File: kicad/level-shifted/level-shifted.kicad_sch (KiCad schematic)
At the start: 7 parts, among them J104 PAL-1 Expansion Connector, SW101 PICO RESET, SW102 SW_DIP_x01, U104 Pico

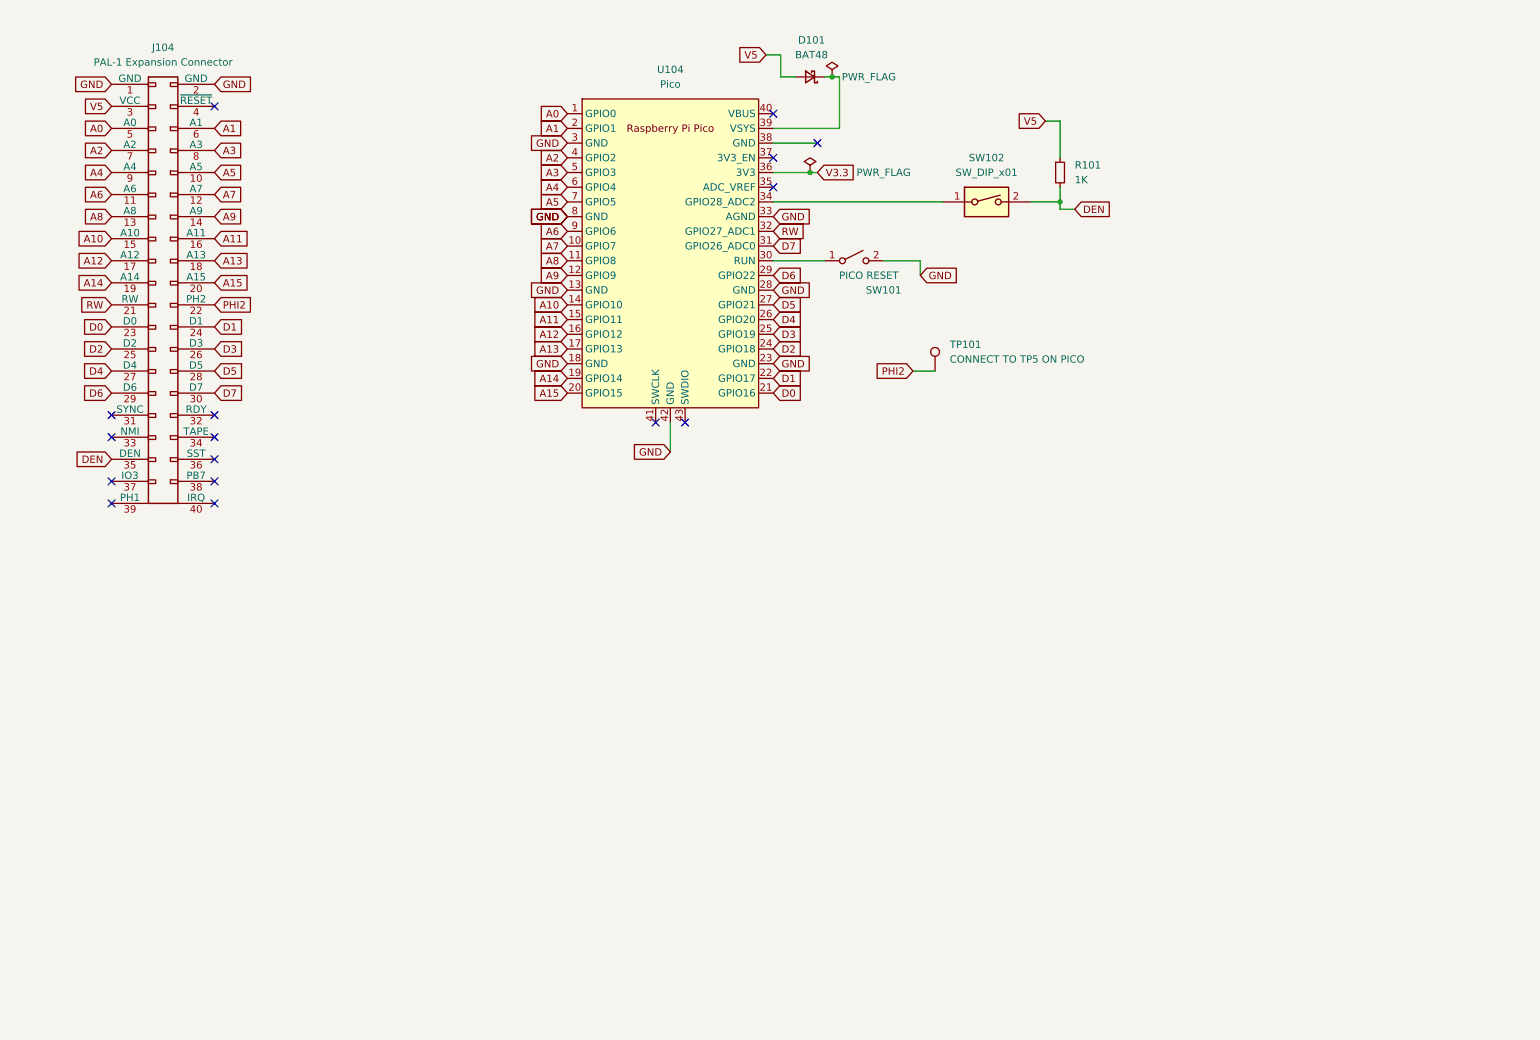
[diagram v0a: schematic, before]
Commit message: New board prepared with the level shifters in place
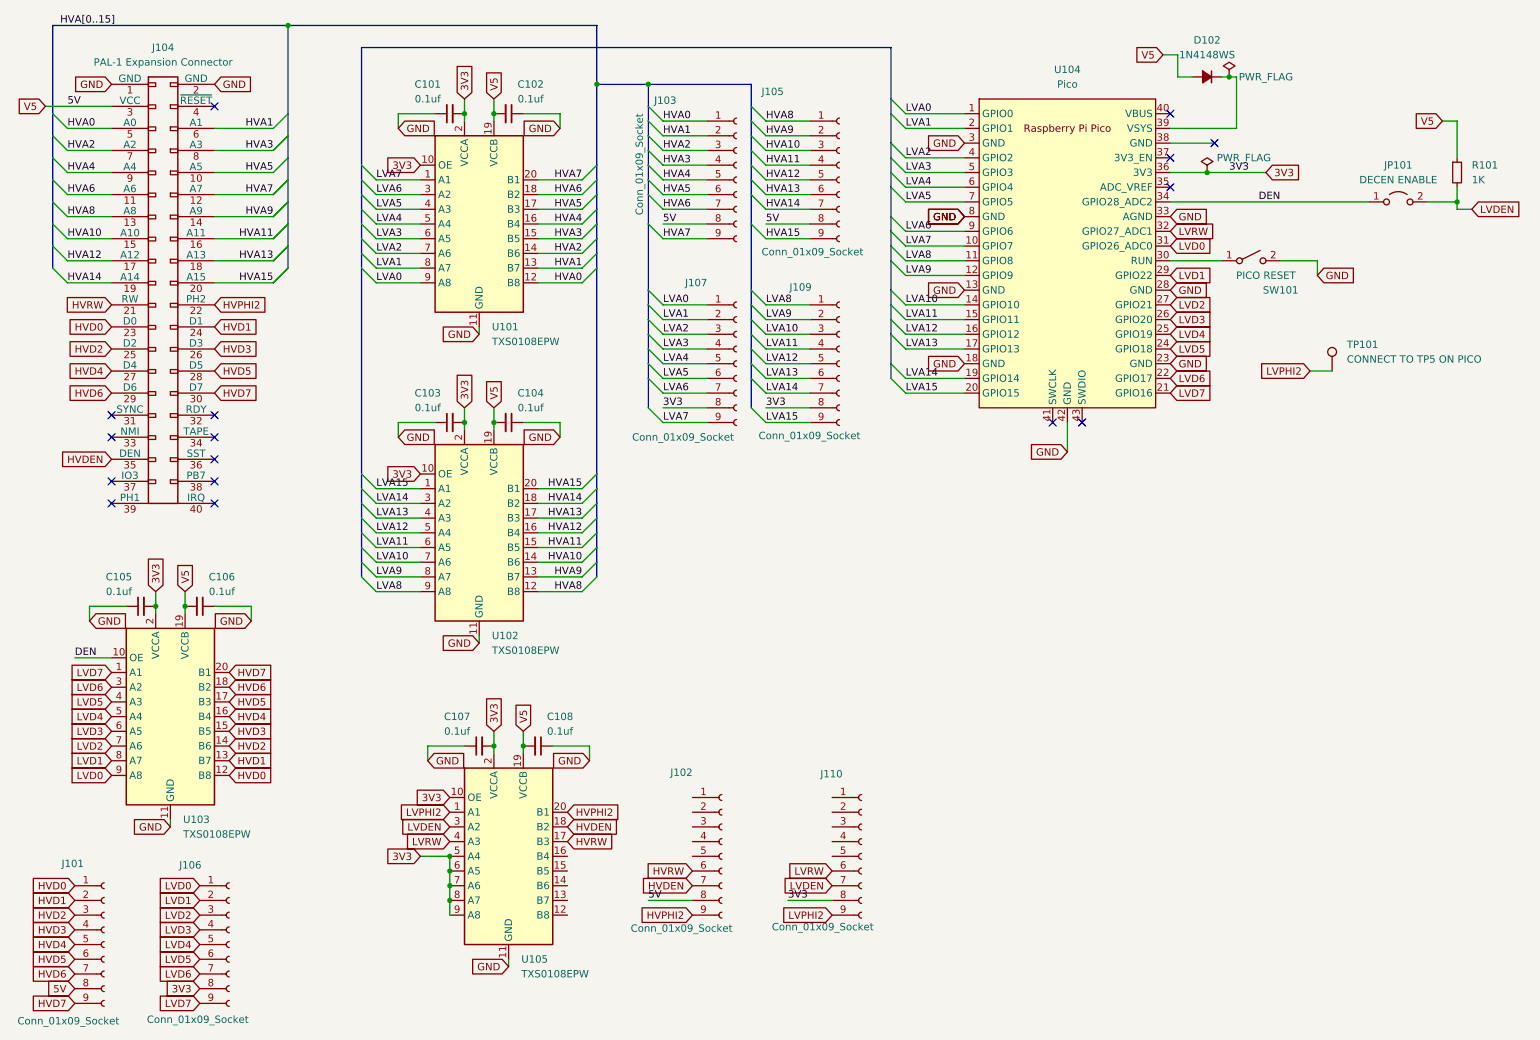
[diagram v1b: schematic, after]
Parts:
- removed D101: BAT48, Diode_THT:D_5W_P10.16mm_Horizontal, symbol Device:D_Schottky_Small
- removed SW102: SW_DIP_x01, Button_Switch_THT:SW_DIP_SPSTx01_Slide_9.78x4.72mm_W7.62mm_P2.54mm, symbol Switch:SW_DIP_x01
- added C101, C102, C103, C104, C105, C106, C107, C108: 0.1uf, Capacitor_SMD:C_0603_1608Metric_Pad1.08x0.95mm_HandSolder, symbol Device:C_Small
- added D102: 1N4148WS, Diode_SMD:D_SOD-323F, symbol Device:D_Small_Filled
- added J101, J102, J103, J105, J106, J107, J109, J110: Conn_01x09_Socket, Connector_PinHeader_1.27mm:PinHeader_1x09_P1.27mm_Vertical, symbol Connector:Conn_01x09_Socket
- added JP101: DECEN ENABLE, Jumper:SolderJumper-2_P1.3mm_Open_RoundedPad1.0x1.5mm, symbol Jumper:Jumper_2_Open
- added U101, U102, U103, U105: TXS0108EPW, Package_SO:TSSOP-20_4.4x6.5mm_P0.65mm, symbol Logic_LevelTranslator:TXS0108EPW
- R101: footprint Resistor_THT:R_Axial_DIN0207_L6.3mm_D2.5mm_P10.16mm_Horizontal -> Resistor_SMD:R_0603_1608Metric_Pad0.98x0.95mm_HandSolder
- SW101: footprint Button_Switch_THT:SW_PUSH_6mm -> Button_Switch_SMD:SW_Push_1P1T_XKB_TS-1187A; JLCPCB (none) -> C2845316; MFG (none) -> HCTL; MFG# (none) -> TC-6601-6-260G
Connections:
- net DEN: now also U104.34 (GPIO28_ADC2), JP101.1 (A), U103.10 (OE); no longer J104.35 (DEN), R101.2
- net GND: now also C101.1, C102.1, C103.1, C104.1, C105.1, C106.1, C107.1, C108.1, U101.11 (GND), U102.11 (GND), U103.11 (GND), U105.11 (GND)
- net at U104.39 (VSYS): now also D102.1 (K)
- net A0 renamed HVA0
- net HVA0: now also J103.1 (Pin_1), U101.12 (B8); no longer U104.1 (GPIO0)
- net A1 renamed HVA1
- net HVA1: now also J103.2 (Pin_2), U101.13 (B7); no longer U104.2 (GPIO1)
- net A10 renamed HVA10
- net HVA10: now also J105.3 (Pin_3), U102.14 (B6); no longer U104.14 (GPIO10)
- net A11 renamed HVA11
- net HVA11: now also J105.4 (Pin_4), U102.15 (B5); no longer U104.15 (GPIO11)
- net A12 renamed HVA12
- net HVA12: now also J105.5 (Pin_5), U102.16 (B4); no longer U104.16 (GPIO12)
- net A13 renamed HVA13
- net HVA13: now also J105.6 (Pin_6), U102.17 (B3); no longer U104.17 (GPIO13)
- net A14 renamed HVA14
- net HVA14: now also J105.7 (Pin_7), U102.18 (B2); no longer U104.19 (GPIO14)
- net A15 renamed HVA15
- net HVA15: now also J105.9 (Pin_9), U102.20 (B1); no longer U104.20 (GPIO15)
- net A2 renamed HVA2
- net HVA2: now also J103.3 (Pin_3), U101.14 (B6); no longer U104.4 (GPIO2)
- net A3 renamed HVA3
- net HVA3: now also J103.4 (Pin_4), U101.15 (B5); no longer U104.5 (GPIO3)
- net A4 renamed HVA4
- net HVA4: now also J103.5 (Pin_5), U101.16 (B4); no longer U104.6 (GPIO4)
- net A5 renamed HVA5
- net HVA5: now also J103.6 (Pin_6), U101.17 (B3); no longer U104.7 (GPIO5)
- net A6 renamed HVA6
- net HVA6: now also J103.7 (Pin_7), U101.18 (B2); no longer U104.9 (GPIO6)
- net A7 renamed HVA7
- net HVA7: now also J103.9 (Pin_9), U101.20 (B1); no longer U104.10 (GPIO7)
- net A8 renamed HVA8
- net HVA8: now also J105.1 (Pin_1), U102.12 (B8); no longer U104.11 (GPIO8)
- net A9 renamed HVA9
- net HVA9: now also J105.2 (Pin_2), U102.13 (B7); no longer U104.12 (GPIO9)
- net D0 renamed HVD0
- net HVD0: now also J101.1 (Pin_1), U103.12 (B8); no longer U104.21 (GPIO16)
- net D1 renamed HVD1
- net HVD1: now also J101.2 (Pin_2), U103.13 (B7); no longer U104.22 (GPIO17)
- net D2 renamed HVD2
- net HVD2: now also J101.3 (Pin_3), U103.14 (B6); no longer U104.24 (GPIO18)
- net D3 renamed HVD3
- net HVD3: now also J101.4 (Pin_4), U103.15 (B5); no longer U104.25 (GPIO19)
- net D4 renamed HVD4
- net HVD4: now also J101.5 (Pin_5), U103.16 (B4); no longer U104.26 (GPIO20)
- net D5 renamed HVD5
- net HVD5: now also J101.6 (Pin_6), U103.17 (B3); no longer U104.27 (GPIO21)
- net D6 renamed HVD6
- net HVD6: now also J101.7 (Pin_7), U103.18 (B2); no longer U104.29 (GPIO22)
- net D7 renamed HVD7
- net HVD7: now also J101.9 (Pin_9), U103.20 (B1); no longer U104.31 (GPIO26_ADC0)
- net PHI2 renamed HVPHI2
- net HVPHI2: now also J102.9 (Pin_9), U105.20 (B1); no longer TP101.1
- net RW renamed HVRW
- net HVRW: now also J102.6 (Pin_6), U105.17 (B3); no longer U104.32 (GPIO27_ADC1)
- net V3.3 renamed 3V3
- net 3V3: now also C101.2, C103.2, C105.2, C107.2, J106.8 (Pin_8), J107.8 (Pin_8), J109.8 (Pin_8), J110.8 (Pin_8), U101.10 (OE), U101.2 (VCCA), U102.10 (OE), U102.2 (VCCA), U103.2 (VCCA), U105.10 (OE), U105.2 (VCCA), U105.5 (A4), U105.6 (A5), U105.7 (A6), U105.8 (A7), U105.9 (A8)
- net V5 renamed 5V
- net 5V: now also C102.2, C104.2, C106.2, C108.2, D102.2 (A), J101.8 (Pin_8), J102.8 (Pin_8), J103.8 (Pin_8), J105.8 (Pin_8), U101.19 (VCCB), U102.19 (VCCB), U103.19 (VCCB), U105.19 (VCCB)
- new net HVDEN: J102.7 (Pin_7), J104.35 (DEN), U105.18 (B2)
- new net LVA0: J107.1 (Pin_1), U101.9 (A8), U104.1 (GPIO0)
- new net LVA1: J107.2 (Pin_2), U101.8 (A7), U104.2 (GPIO1)
- new net LVA10: J109.3 (Pin_3), U102.7 (A6), U104.14 (GPIO10)
- new net LVA11: J109.4 (Pin_4), U102.6 (A5), U104.15 (GPIO11)
- new net LVA12: J109.5 (Pin_5), U102.5 (A4), U104.16 (GPIO12)
- new net LVA13: J109.6 (Pin_6), U102.4 (A3), U104.17 (GPIO13)
- new net LVA14: J109.7 (Pin_7), U102.3 (A2), U104.19 (GPIO14)
- new net LVA15: J109.9 (Pin_9), U102.1 (A1), U104.20 (GPIO15)
- new net LVA2: J107.3 (Pin_3), U101.7 (A6), U104.4 (GPIO2)
- new net LVA3: J107.4 (Pin_4), U101.6 (A5), U104.5 (GPIO3)
- new net LVA4: J107.5 (Pin_5), U101.5 (A4), U104.6 (GPIO4)
- new net LVA5: J107.6 (Pin_6), U101.4 (A3), U104.7 (GPIO5)
- new net LVA6: J107.7 (Pin_7), U101.3 (A2), U104.9 (GPIO6)
- new net LVA7: J107.9 (Pin_9), U101.1 (A1), U104.10 (GPIO7)
- new net LVA8: J109.1 (Pin_1), U102.9 (A8), U104.11 (GPIO8)
- new net LVA9: J109.2 (Pin_2), U102.8 (A7), U104.12 (GPIO9)
- new net LVD0: J106.1 (Pin_1), U103.9 (A8), U104.31 (GPIO26_ADC0)
- new net LVD1: J106.2 (Pin_2), U103.8 (A7), U104.29 (GPIO22)
- new net LVD2: J106.3 (Pin_3), U103.7 (A6), U104.27 (GPIO21)
- new net LVD3: J106.4 (Pin_4), U103.6 (A5), U104.26 (GPIO20)
- new net LVD4: J106.5 (Pin_5), U103.5 (A4), U104.25 (GPIO19)
- new net LVD5: J106.6 (Pin_6), U103.4 (A3), U104.24 (GPIO18)
- new net LVD6: J106.7 (Pin_7), U103.3 (A2), U104.22 (GPIO17)
- new net LVD7: J106.9 (Pin_9), U103.1 (A1), U104.21 (GPIO16)
- new net LVDEN: J110.7 (Pin_7), JP101.2 (B), R101.2, U105.3 (A2)
- new net LVPHI2: J110.9 (Pin_9), TP101.1, U105.1 (A1)
- new net LVRW: J110.6 (Pin_6), U104.32 (GPIO27_ADC1), U105.4 (A3)
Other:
- moved on the sheet: R101, SW101, TP101, U104
